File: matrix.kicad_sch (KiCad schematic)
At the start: 101 parts, among them SW1 SW_Push_45deg, SW10 SW_Push_45deg, SW11 SW_Push_45deg, SW12 SW_Push_45deg, SW12(1.5)1 SW_Push_45deg, SW13 SW_Push_45deg, SW13(1.5)1 SW_Push_45deg, SW14 SW_Push_45deg, SW14(1.25)1 SW_Push_45deg, SW15 SW_Push_45deg, SW16 SW_Push_45deg, SW17 SW_Push_45deg, SW18 SW_Push_45deg, SW19 SW_Push_45deg, SW2 SW_Push_45deg, SW20 SW_Push_45deg, SW21 SW_Push_45deg, SW22 SW_Push_45deg, SW23 SW_Push_45deg, SW24 SW_Push_45deg, SW25 SW_Push_45deg, SW26 SW_Push_45deg, SW26a1 SW_Push_45deg, SW26b1 SW_Push_45deg, SW27 SW_Push_45deg, SW28 SW_Push_45deg, SW29 SW_Push_45deg, SW3 SW_Push_45deg, SW30 SW_Push_45deg, SW31 SW_Push_45deg, SW32 SW_Push_45deg, SW33 SW_Push_45deg, SW34 SW_Push_45deg, SW35 SW_Push_45deg, SW36 SW_Push_45deg, SW37(1.75)1 SW_Push_45deg, SW37(2.75)1 SW_Push_45deg, SW38 RotaryEncoder_Switch, SW39 SW_Push_45deg, SW4 SW_Push_45deg, SW40 SW_Push_45deg, SW40(1.5)1 SW_Push_45deg, SW41 SW_Push_45deg, SW41(1)1 SW_Push_45deg, SW42 SW_Push_45deg, SW42a1 SW_Push_45deg, SW43 SW_Push_45deg, SW44 SW_Push_45deg, SW44a1 SW_Push_45deg, SW45 SW_Push_45deg, SW45a1 SW_Push_45deg, SW5 SW_Push_45deg, SW6 SW_Push_45deg, SW7 SW_Push_45deg, SW8 SW_Push_45deg, SW9 SW_Push_45deg

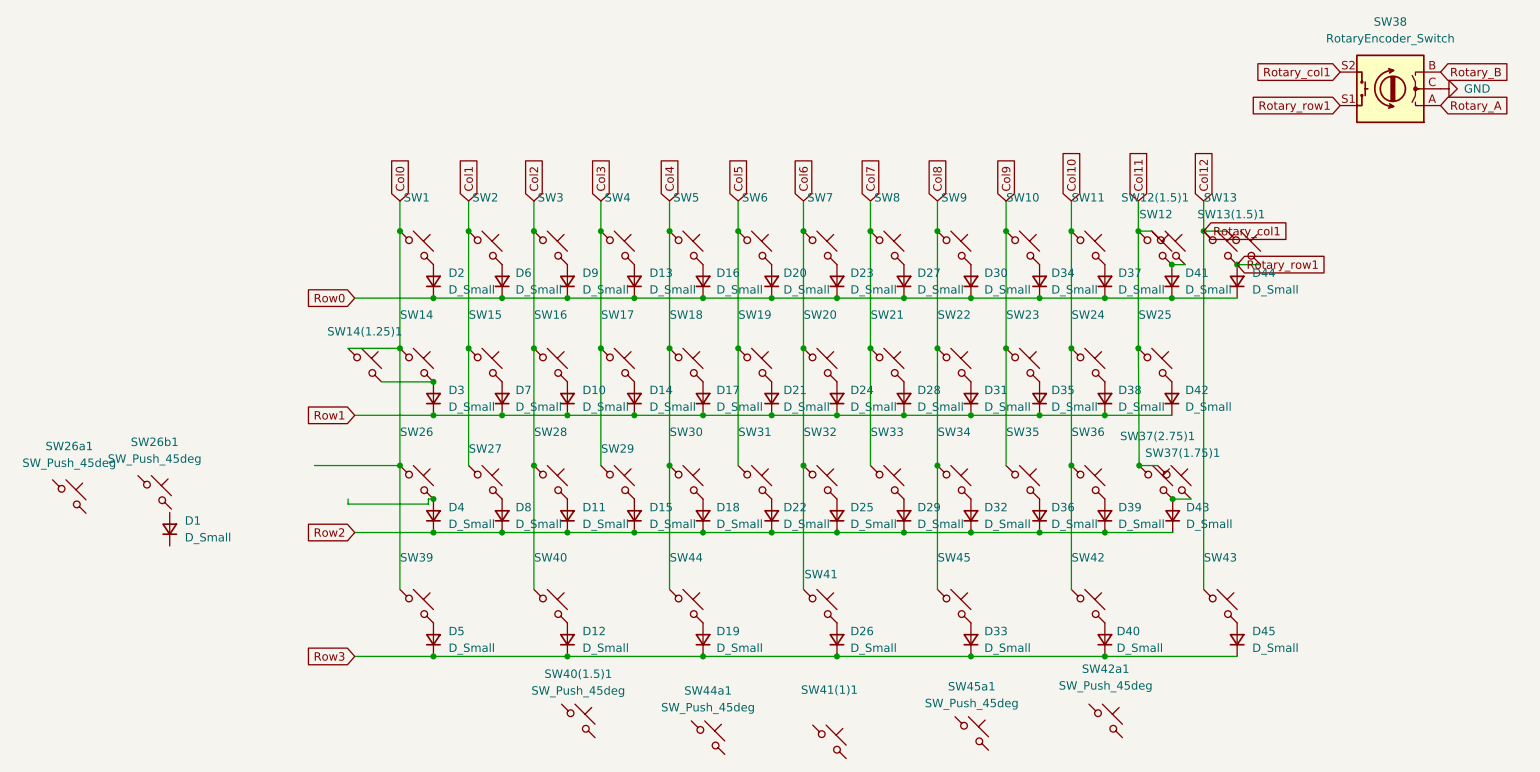
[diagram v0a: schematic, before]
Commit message: removed underglow, cleaned some routing, fixed errors
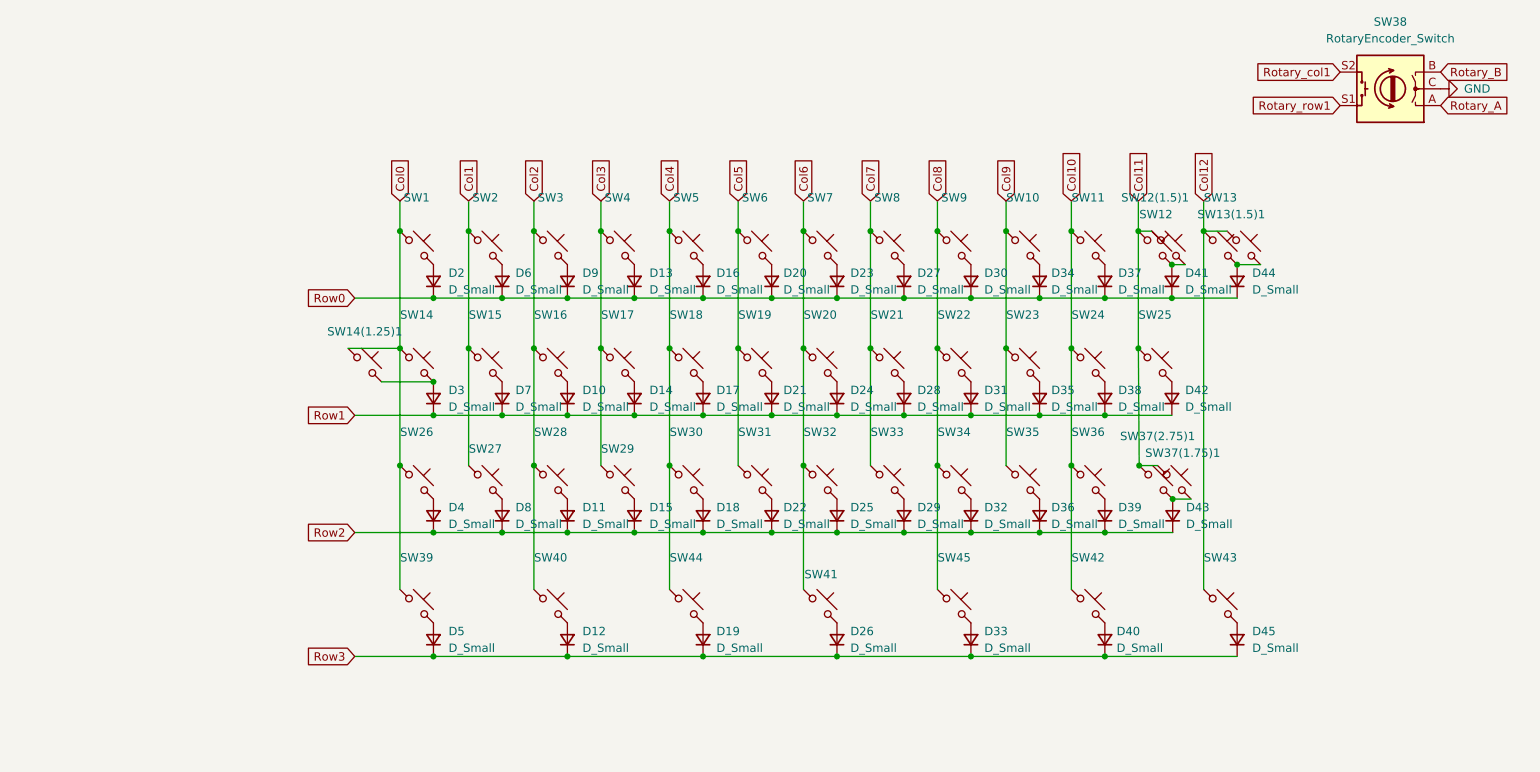
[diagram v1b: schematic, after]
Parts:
- removed D1: D_Small, Diode_SMD:D_SOD-123F, symbol Device:D_Small
- removed SW26a1: SW_Push_45deg, MX_Only:MXOnly-1.25U-NoLED, symbol Switch:SW_Push_45deg
- removed SW26b1, SW41(1)1: SW_Push_45deg, MX_Only:MXOnly-1U-NoLED, symbol Switch:SW_Push_45deg
- removed SW40(1.5)1, SW42a1: SW_Push_45deg, MX_Only:MXOnly-1.5U-NoLED, symbol Switch:SW_Push_45deg
- removed SW44a1, SW45a1: SW_Push_45deg, MX_Only:MXOnly-3U-ReversedStabilizers-NoLED, symbol Switch:SW_Push_45deg
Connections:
- net Col12: no longer SW38.S2
- net Rotary_row1: no longer D44.2 (A), SW13(1.5)1.2, SW13.2
- new net: D44.2 (A), SW13(1.5)1.2, SW13.2
- new net Rotary_col1: SW38.S2
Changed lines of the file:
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@@
   (junction (at 118.364 115.316) (diameter 0) (color 0 0 0 0)
   )
-  (junction (at 98.044 91.44) (diameter 0) (color 0 0 0 0)
-  )
   (junction (at 174.498 86.36) (diameter 0) (color 0 0 0 0)
   )
@@
     (stroke (width 0) (type default) (color 0 0 0 0))
   )
-  (wire (pts (xy 85.09 91.44) (xy 85.09 92.202))
-    (stroke (width 0) (type default) (color 0 0 0 0))
-  )
   (wire (pts (xy 128.524 78.74) (xy 138.938 78.74))
     (stroke (width 0) (type default) (color 0 0 0 0))
@@
     (stroke (width 0) (type default) (color 0 0 0 0))
   )
-  (wire (pts (xy 80.01 86.36) (xy 92.964 86.36))
-    (stroke (width 0) (type default) (color 0 0 0 0))
-  )
   (wire (pts (xy 144.272 50.8) (xy 144.272 68.58))
     (stroke (width 0) (type default) (color 0 0 0 0))
@@
     (stroke (width 0) (type default) (color 0 0 0 0))
   )
-  (wire (pts (xy 85.09 92.202) (xy 97.282 92.202))
-    (stroke (width 0) (type default) (color 0 0 0 0))
-  )
   (wire (pts (xy 154.178 68.58) (xy 154.178 86.36))
     (stroke (width 0) (type default) (color 0 0 0 0))
@@
     (stroke (width 0) (type default) (color 0 0 0 0))
   )
-  (wire (pts (xy 97.282 91.44) (xy 98.044 91.44))
-    (stroke (width 0) (type default) (color 0 0 0 0))
-  )
   (wire (pts (xy 98.044 96.52) (xy 108.458 96.52))
     (stroke (width 0) (type default) (color 0 0 0 0))
@@
   )
   (wire (pts (xy 98.044 115.316) (xy 118.364 115.316))
-    (stroke (width 0) (type default) (color 0 0 0 0))
-  )
-  (wire (pts (xy 97.282 92.202) (xy 97.282 91.44))
     (stroke (width 0) (type default) (color 0 0 0 0))
   )
@@
     (property "Intersheet References" "${INTERSHEET_REFS}" (id 0) (at 78.7339 78.6606 0)
       (effects (font (size 1.27 1.27)) (justify right) hide)
-    )
-  )
-  (global_label "Rotary_col1" (shape input) (at 214.884 50.8 0) (fields_autoplaced)
-    (effects (font (size 1.27 1.27)) (justify left))
-    (property "Intersheet References" "${INTERSHEET_REFS}" (id 0) (at 228.4247 50.8794 0)
-      (effects (font (size 1.27 1.27)) (justify left) hide)
-    )
-  )
-  (global_label "Rotary_row1" (shape input) (at 219.964 55.88 0) (fields_autoplaced)
-    (effects (font (size 1.27 1.27)) (justify left))
-    (property "Intersheet References" "${INTERSHEET_REFS}" (id 0) (at 233.8676 55.9594 0)
-      (effects (font (size 1.27 1.27)) (justify left) hide)
     )
   )
@@
     (pin "2")
   )
-  (symbol (lib_id "Switch:SW_Push_45deg") (at 200.025 125.095 0) (unit 1)
-    (in_bom no) (on_board no) (fields_autoplaced)
-    (property "Reference" "SW42a1" (id 0) (at 200.025 117.221 0))
-    (property "Value" "SW_Push_45deg" (id 1) (at 200.025 119.761 0))
-    (property "Footprint" "MX_Only:MXOnly-1.5U-NoLED" (id 2) (at 200.025 125.095 0)
-      (effects (font (size 1.27 1.27)) hide)
-    )
-    (property "Datasheet" "~" (id 3) (at 200.025 125.095 0)
-      (effects (font (size 1.27 1.27)) hide)
-    )
-    (pin "1")
-    (pin "2")
-  )
   (symbol (lib_id "Switch:SW_Push_45deg") (at 146.812 88.9 0) (unit 1)
     (in_bom yes) (on_board yes) (fields_autoplaced)
@@
     (pin "2")
   )
-  (symbol (lib_id "Switch:SW_Push_45deg") (at 139.7 127.635 0) (unit 1)
-    (in_bom no) (on_board no) (fields_autoplaced)
-    (property "Reference" "SW44a1" (id 0) (at 139.7 120.523 0))
-    (property "Value" "SW_Push_45deg" (id 1) (at 139.7 123.063 0))
-    (property "Footprint" "MX_Only:MXOnly-3U-ReversedStabilizers-NoLED" (id 2) (at 139.7 127.635 0)
-      (effects (font (size 1.27 1.27)) hide)
-    )
-    (property "Datasheet" "~" (id 3) (at 139.7 127.635 0)
-      (effects (font (size 1.27 1.27)) hide)
-    )
-    (pin "1")
-    (pin "2")
-  )
   (symbol (lib_id "Switch:SW_Push_45deg") (at 156.718 53.34 0) (unit 1)
     (in_bom yes) (on_board yes) (fields_autoplaced)
@@
     (pin "2")
   )
-  (symbol (lib_id "Device:D_Small") (at 58.039 96.012 90) (unit 1)
-    (in_bom no) (on_board no) (fields_autoplaced)
-    (property "Reference" "D1" (id 0) (at 60.325 94.7419 90)
-      (effects (font (size 1.27 1.27)) (justify right))
-    )
-    (property "Value" "D_Small" (id 1) (at 60.325 97.2819 90)
-      (effects (font (size 1.27 1.27)) (justify right))
-    )
-    (property "Footprint" "Diode_SMD:D_SOD-123F" (id 2) (at 58.039 96.012 90)
-      (effects (font (size 1.27 1.27)) hide)
-    )
-    (property "Datasheet" "~" (id 3) (at 58.039 96.012 90)
-      (effects (font (size 1.27 1.27)) hide)
-    )
-    (pin "1")
-    (pin "2")
-  )
   (symbol (lib_id "Device:D_Small") (at 199.898 93.98 90) (unit 1)
     (in_bom yes) (on_board yes) (fields_autoplaced)
@@
     )
     (property "Datasheet" "~" (id 3) (at 136.398 71.12 0)
-      (effects (font (size 1.27 1.27)) hide)
-    )
-    (pin "1")
-    (pin "2")
-  )
-  (symbol (lib_id "Switch:SW_Push_45deg") (at 120.015 125.095 0) (unit 1)
-    (in_bom no) (on_board no) (fields_autoplaced)
-    (property "Reference" "SW40(1.5)1" (id 0) (at 120.015 117.983 0))
-    (property "Value" "SW_Push_45deg" (id 1) (at 120.015 120.523 0))
-    (property "Footprint" "MX_Only:MXOnly-1.5U-NoLED" (id 2) (at 120.015 125.095 0)
-      (effects (font (size 1.27 1.27)) hide)
-    )
-    (property "Datasheet" "~" (id 3) (at 120.015 125.095 0)
-      (effects (font (size 1.27 1.27)) hide)
-    )
-    (pin "1")
-    (pin "2")
-  )
-  (symbol (lib_id "Switch:SW_Push_45deg") (at 179.705 127 0) (unit 1)
-    (in_bom no) (on_board no) (fields_autoplaced)
-    (property "Reference" "SW45a1" (id 0) (at 179.705 119.888 0))
-    (property "Value" "SW_Push_45deg" (id 1) (at 179.705 122.428 0))
-    (property "Footprint" "MX_Only:MXOnly-3U-ReversedStabilizers-NoLED" (id 2) (at 179.705 127 0)
-      (effects (font (size 1.27 1.27)) hide)
-    )
-    (property "Datasheet" "~" (id 3) (at 179.705 127 0)
       (effects (font (size 1.27 1.27)) hide)
     )
@@
     (pin "2")
   )
-  (symbol (lib_id "Switch:SW_Push_45deg") (at 55.753 90.424 0) (unit 1)
-    (in_bom no) (on_board no) (fields_autoplaced)
-    (property "Reference" "SW26b1" (id 0) (at 55.753 82.804 0))
-    (property "Value" "SW_Push_45deg" (id 1) (at 55.753 85.344 0))
-    (property "Footprint" "MX_Only:MXOnly-1U-NoLED" (id 2) (at 55.753 90.424 0)
-      (effects (font (size 1.27 1.27)) hide)
-    )
-    (property "Datasheet" "~" (id 3) (at 55.753 90.424 0)
-      (effects (font (size 1.27 1.27)) hide)
-    )
-    (pin "1")
-    (pin "2")
-  )
   (symbol (lib_id "Device:D_Small") (at 108.458 58.42 90) (unit 1)
     (in_bom yes) (on_board yes) (fields_autoplaced)
@@
       (effects (font (size 1.27 1.27)) hide)
     )
-    (pin "1")
-    (pin "2")
-  )
-  (symbol (lib_id "Switch:SW_Push_45deg") (at 158.115 128.27 0) (unit 1)
-    (in_bom no) (on_board no) (fields_autoplaced)
-    (property "Reference" "SW41(1)1" (id 0) (at 158.115 120.396 0))
-    (property "Value" "SW_Push_45deg" (id 1) (at 158.115 122.936 0)
-      (effects (font (size 1.27 1.27)) hide)
-    )
-    (property "Footprint" "MX_Only:MXOnly-1U-NoLED" (id 2) (at 158.115 128.27 0)
-      (effects (font (size 1.27 1.27)) hide)
-    )
-    (property "Datasheet" "~" (id 3) (at 158.115 128.27 0)
-      (effects (font (size 1.27 1.27)) hide)
-    )
-    (pin "1")
-    (pin "2")
-  )
-  (symbol (lib_id "Switch:SW_Push_45deg") (at 42.799 91.059 0) (unit 1)
-    (in_bom no) (on_board no) (fields_autoplaced)
-    (property "Reference" "SW26a1" (id 0) (at 42.799 83.439 0))
-    (property "Value" "SW_Push_45deg" (id 1) (at 42.799 85.979 0))
-    (property "Footprint" "MX_Only:MXOnly-1.25U-NoLED" (id 2) (at 42.799 91.059 0)
-      (effects (font (size 1.27 1.27)) hide)
-    )
-    (property "Datasheet" "~" (id 3) (at 42.799 91.059 0)
-      (effects (font (size 1.27 1.27)) hide)
-    )

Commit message: quick schematics cleanup
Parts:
- removed SW38: RotaryEncoder_Switch, Keebio-Parts:RotaryEncoder_EC11-no-legs, symbol Device:RotaryEncoder_Switch
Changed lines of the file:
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@@
-    )
-  )
-  (global_label "Rotary_B" (shape input) (at 250.825 26.67 0) (fields_autoplaced)
-    (effects (font (size 1.27 1.27)) (justify left))
-    (property "Intersheet References" "${INTERSHEET_REFS}" (id 0) (at 261.5233 26.5906 0)
-      (effects (font (size 1.27 1.27)) (justify left) hide)
     )
   )
@@
     )
   )
-  (global_label "Rotary_A" (shape input) (at 250.825 31.75 0) (fields_autoplaced)
-    (effects (font (size 1.27 1.27)) (justify left))
-    (property "Intersheet References" "${INTERSHEET_REFS}" (id 0) (at 261.3419 31.6706 0)
-      (effects (font (size 1.27 1.27)) (justify left) hide)
-    )
-  )
   (global_label "Col6" (shape input) (at 154.178 46.228 90) (fields_autoplaced)
     (effects (font (size 1.27 1.27)) (justify left))
@@
     )
   )
-  (global_label "Rotary_row1" (shape input) (at 235.585 31.75 180) (fields_autoplaced)
-    (effects (font (size 1.27 1.27)) (justify right))
-    (property "Intersheet References" "${INTERSHEET_REFS}" (id 0) (at 221.6814 31.6706 0)
-      (effects (font (size 1.27 1.27)) (justify right) hide)
-    )
-  )
   (global_label "Row3" (shape input) (at 86.106 115.316 180) (fields_autoplaced)
     (effects (font (size 1.27 1.27)) (justify right))
@@
     )
   )
-  (global_label "Rotary_col1" (shape input) (at 235.585 26.67 180) (fields_autoplaced)
-    (effects (font (size 1.27 1.27)) (justify right))
-    (property "Intersheet References" "${INTERSHEET_REFS}" (id 0) (at 222.0443 26.5906 0)
-      (effects (font (size 1.27 1.27)) (justify right) hide)
-    )
-  )
   (symbol (lib_id "Device:D_Small") (at 108.458 93.98 90) (unit 1)
     (in_bom yes) (on_board yes) (fields_autoplaced)
@@
     (pin "1")
     (pin "2")
-  )
-  (symbol (lib_id "power:GND") (at 250.825 29.21 90) (unit 1)
-    (in_bom yes) (on_board yes) (fields_autoplaced)
-    (property "Reference" "#PWR0101" (id 0) (at 257.175 29.21 0)
-      (effects (font (size 1.27 1.27)) hide)
-    )
-    (property "Value" "GND" (id 1) (at 254.381 29.2099 90)
-      (effects (font (size 1.27 1.27)) (justify right))
-    )
-    (property "Footprint" "" (id 2) (at 250.825 29.21 0)
-      (effects (font (size 1.27 1.27)) hide)
-    )
-    (property "Datasheet" "" (id 3) (at 250.825 29.21 0)
-      (effects (font (size 1.27 1.27)) hide)
-    )
-    (pin "1")
   )
   (symbol (lib_id "Switch:SW_Push_45deg") (at 187.452 53.34 0) (unit 1)
@@
     (pin "2")
   )
-  (symbol (lib_id "Device:RotaryEncoder_Switch") (at 243.205 29.21 180) (unit 1)
-    (in_bom no) (on_board no) (fields_autoplaced)
-    (property "Reference" "SW38" (id 0) (at 243.205 19.05 0))
-    (property "Value" "RotaryEncoder_Switch" (id 1) (at 243.205 21.59 0))
-    (property "Footprint" "Keebio-Parts:RotaryEncoder_EC11-no-legs" (id 2) (at 247.015 33.274 0)
-      (effects (font (size 1.27 1.27)) hide)
-    )
-    (property "Datasheet" "~" (id 3) (at 243.205 35.814 0)
-      (effects (font (size 1.27 1.27)) hide)
-    )
-    (pin "A")
-    (pin "B")
-    (pin "C")
-    (pin "S1")
-    (pin "S2")
-  )
   (symbol (lib_id "Device:D_Small") (at 159.258 76.2 90) (unit 1)
